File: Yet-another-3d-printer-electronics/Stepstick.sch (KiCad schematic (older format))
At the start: 60 parts

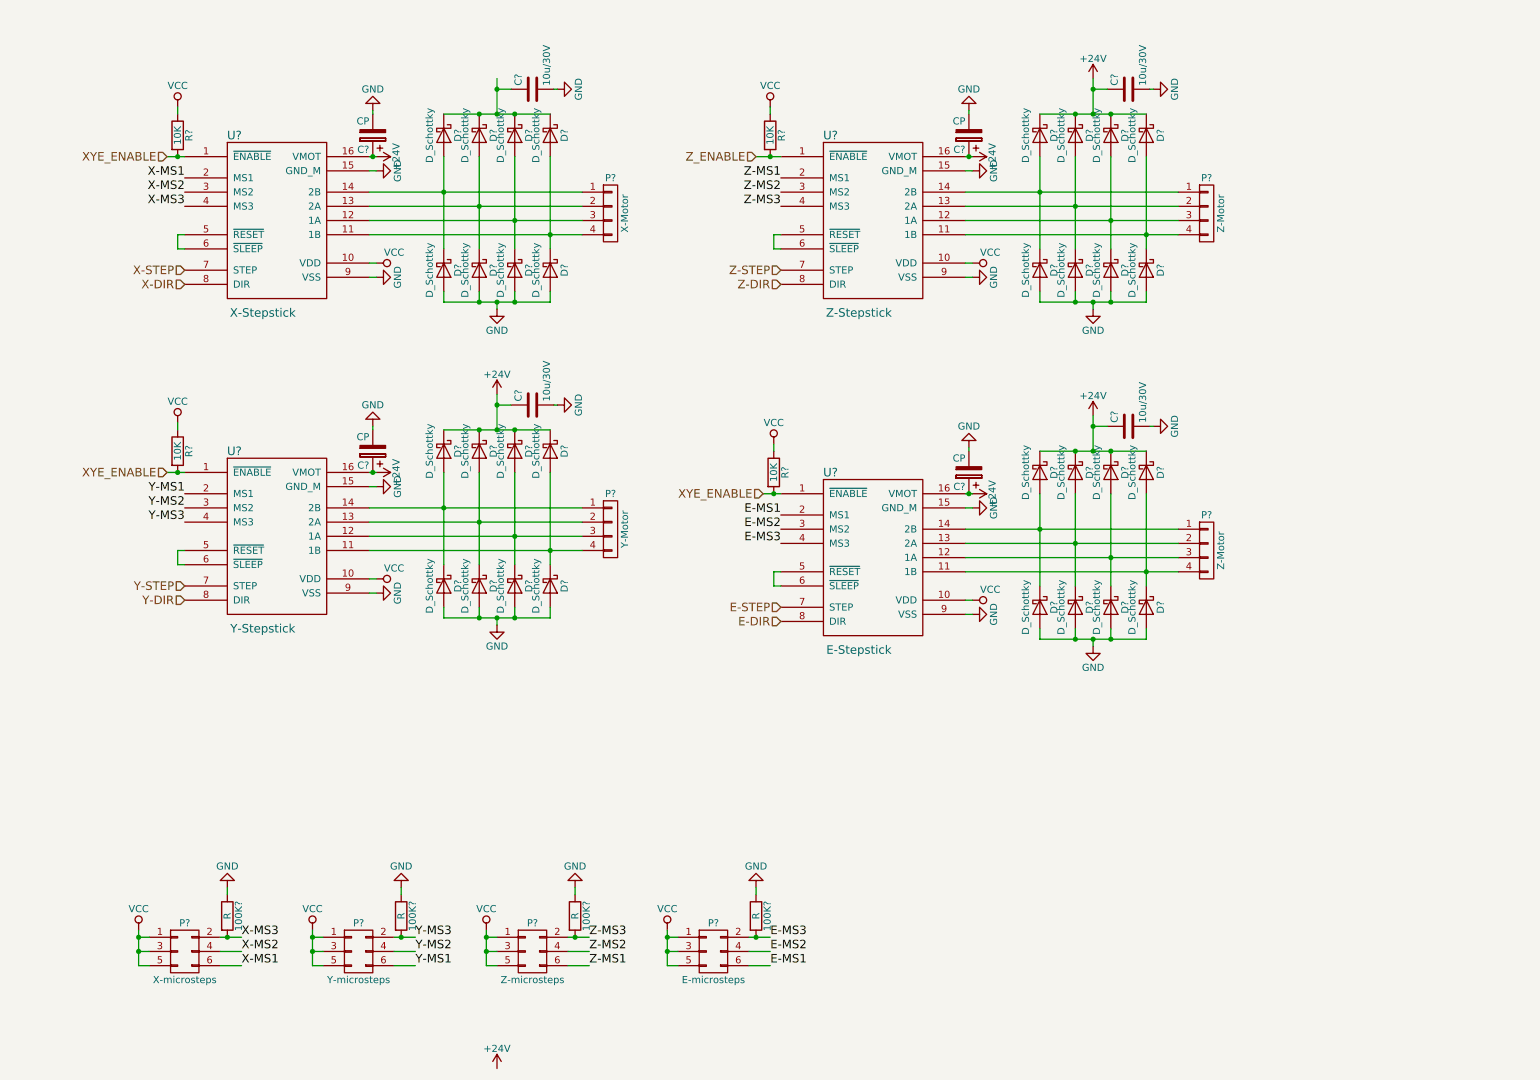
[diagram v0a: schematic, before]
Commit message: Add power section and remove fan heater
Add aoz1284pi buck conventer.

Signed-off-by: Mateusz Krawczuk <mat.krawczuk@gmail.com>
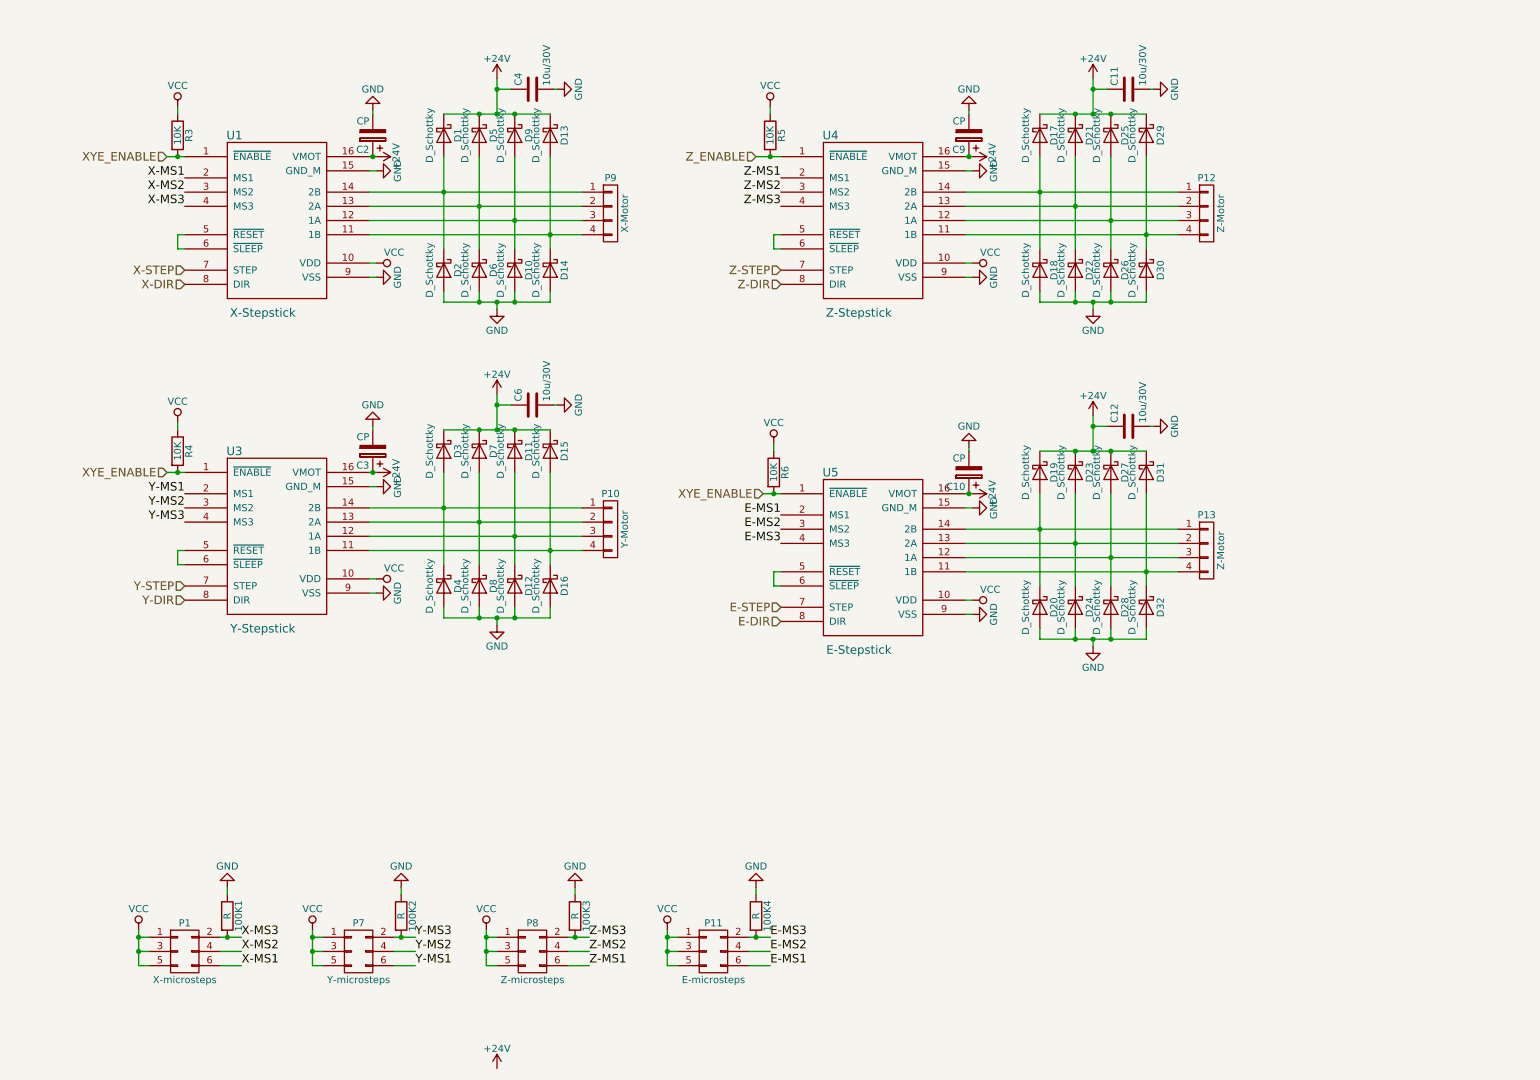
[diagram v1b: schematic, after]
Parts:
- gave numbers to parts that had none: 60
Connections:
- net +24V: now also C4.1, D1.1 (K), D13.1 (K), D5.1 (K), D9.1 (K)

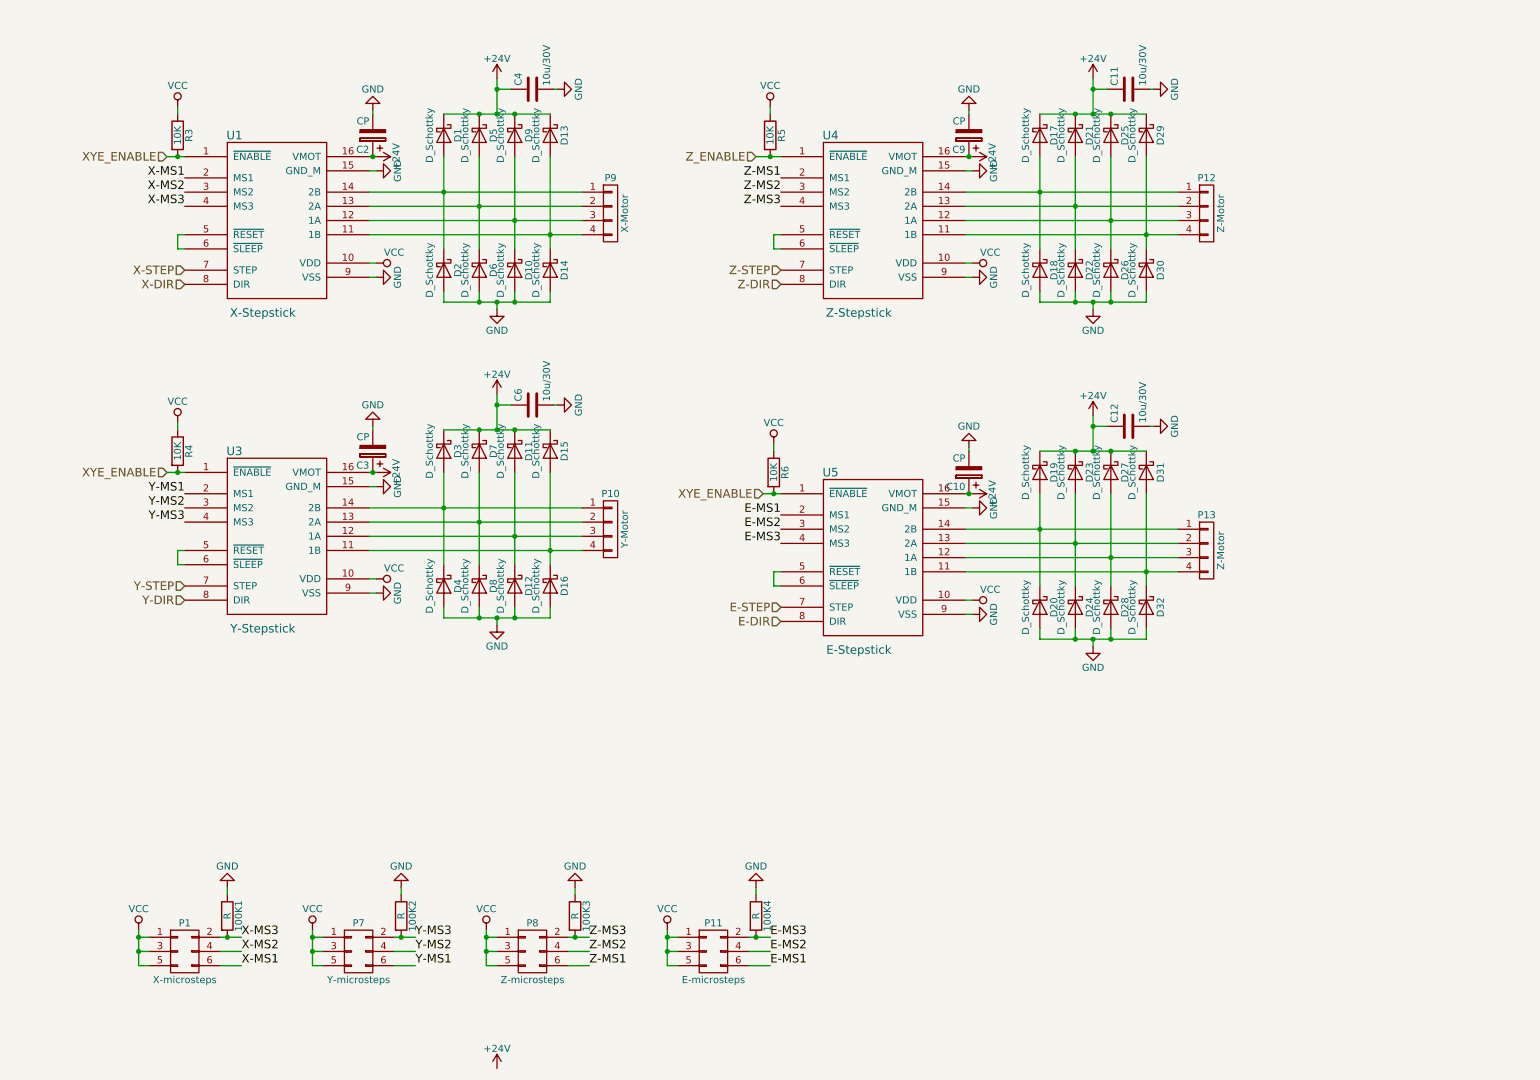
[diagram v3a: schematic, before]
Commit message: Add additional stepstick, hotend fan and heater and temperature sensor
Extruder stepsticks have independ enables pins. Vcc was replace by valid
power source.

Signed-off-by: Mateusz Krawczuk <mat.krawczuk@gmail.com>
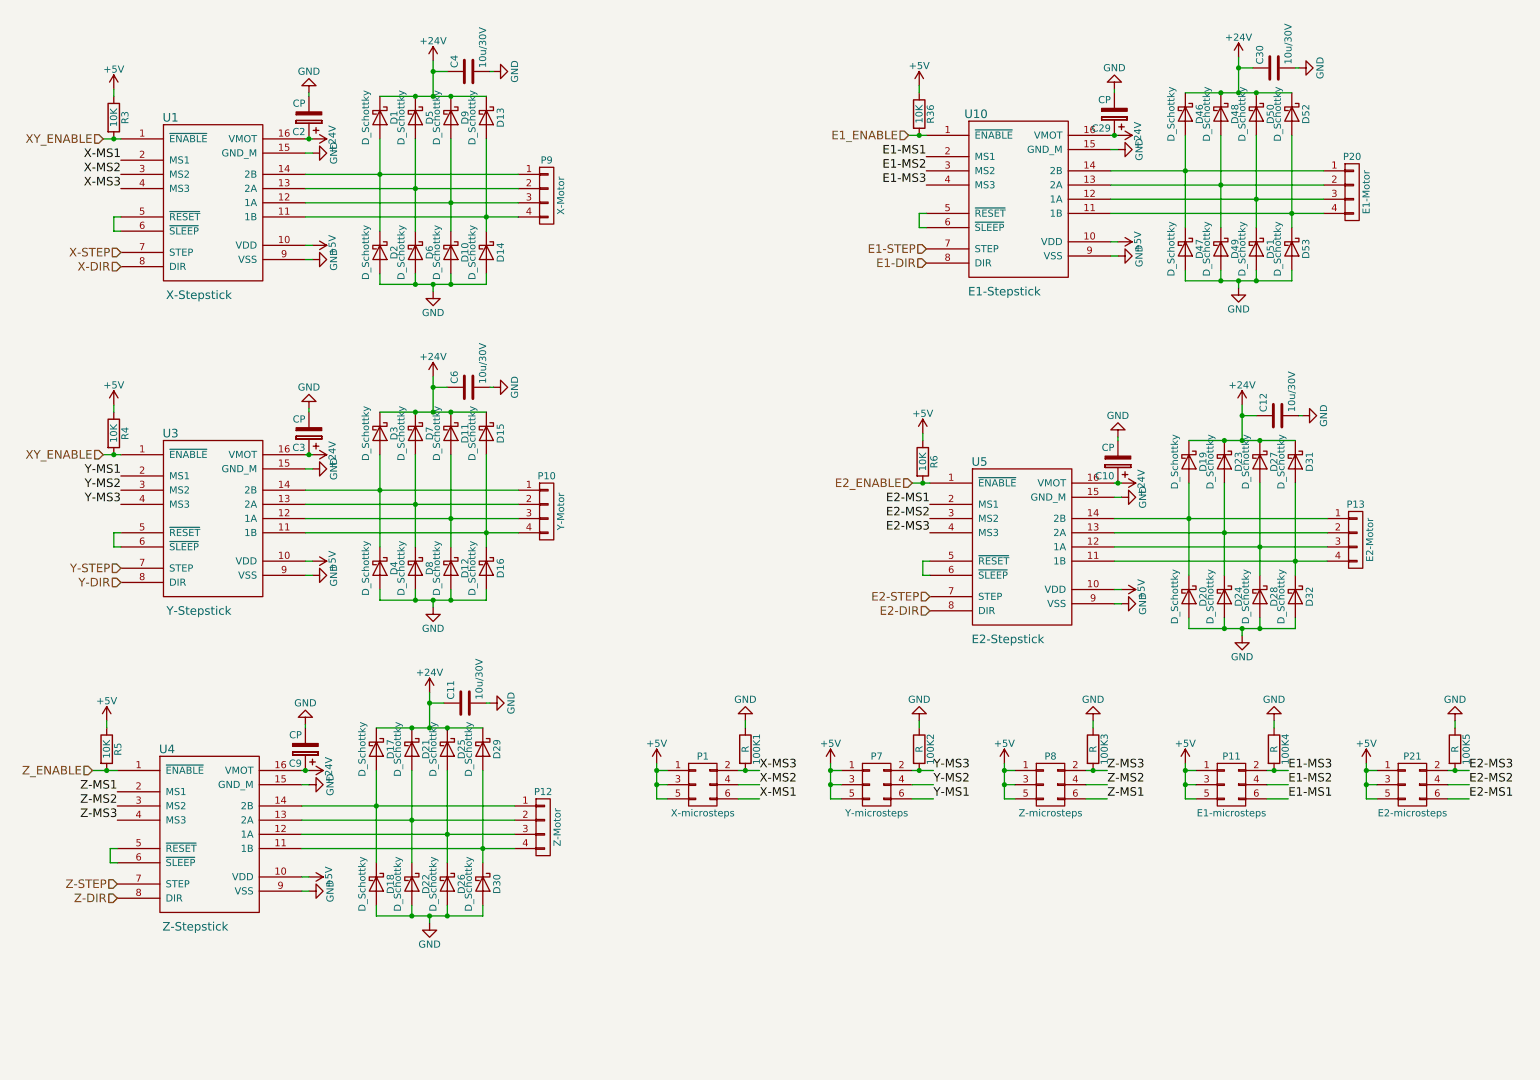
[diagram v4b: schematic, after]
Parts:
- added 100K5: R, Resistors_SMD:R_0805_HandSoldering, symbol R
- added C29: CP, Capacitors_THT:CP_Radial_D5.0mm_P2.00mm, symbol CP
- added C30: 10u/30V, Capacitors_SMD:C_1206_HandSoldering, symbol C
- added D46, D47, D48, D49, D50, D51, D52, D53: D_Schottky, Yet-another-3d-printer-electronics:DO-214AC(SMA), symbol D_Schottky
- added P20: E1-Motor, Connectors_JST:JST_XH_B04B-XH-A_04x2.50mm_Straight, symbol CONN_01X04
- added P21: E2-microsteps, Socket_Strips:Socket_Strip_Straight_2x03_Pitch2.54mm, symbol CONN_02X03
- added R36: 10K, Resistors_SMD:R_0805_HandSoldering, symbol R
- added U10: E1-Stepstick, Yet-another-3d-printer-electronics:stepstick_socket, symbol StepStick
- P11: value E-microsteps -> E1-microsteps
- P13: value Z-Motor -> E2-Motor
- U5: value E-Stepstick -> E2-Stepstick
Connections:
- net +24V: now also C29.1, C30.1, D46.1 (K), D48.1 (K), D50.1 (K), D52.1 (K), U10.16 (VMOT)
- net GND: now also 100K5.1, C29.2, C30.2, D47.2 (A), D49.2 (A), D51.2 (A), D53.2 (A), U10.15 (GND_M), U10.9 (VSS)
- net E-DIR renamed E2-DIR
- net E-MS1 renamed E1-MS1
- net E1-MS1: now also U10.2 (MS1); no longer U5.2 (MS1)
- net E-MS2 renamed E1-MS2
- net E1-MS2: now also U10.3 (MS2); no longer U5.3 (MS2)
- net E-MS3 renamed E1-MS3
- net E1-MS3: now also U10.4 (MS3); no longer U5.4 (MS3)
- net E-STEP renamed E2-STEP
- net VCC renamed +5V
- net +5V: now also P21.1 (P1), P21.3 (P3), P21.5 (P5), R36.1, U10.10 (VDD)
- net XYE_ENABLE renamed XY_ENABLE
- net XY_ENABLE: no longer R6.2, U5.1 (~ENABLE)
- new net: D46.2 (A), D47.1 (K), P20.1 (P1), U10.14 (2B)
- new net: D52.2 (A), D53.1 (K), P20.4 (P4), U10.11 (1B)
- new net: D50.2 (A), D51.1 (K), P20.3 (P3), U10.12 (1A)
- new net: D48.2 (A), D49.1 (K), P20.2 (P2), U10.13 (2A)
- new net: U10.5 (~RESET), U10.6 (~SLEEP)
- new net E1-DIR: U10.8 (DIR)
- new net E1-STEP: U10.7 (STEP)
- new net E1_ENABLE: R36.2, U10.1 (~ENABLE)
- new net E2-MS1: P21.6 (P6), U5.2 (MS1)
- new net E2-MS2: P21.4 (P4), U5.3 (MS2)
- new net E2-MS3: 100K5.2, P21.2 (P2), U5.4 (MS3)
- new net E2_ENABLE: R6.2, U5.1 (~ENABLE)
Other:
- moved on the sheet: 100K1, 100K2, 100K3, 100K4, C10, C11, C12, C2, C3, C4, C6, C9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

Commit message: Choose footprints for some components
Signed-off-by: Mateusz Krawczuk <mat.krawczuk@gmail.com>
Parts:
- R3, R36, R4, R5, R6: footprint Resistors_SMD:R_0805_HandSoldering -> Resistors_SMD:R_0603_HandSoldering
